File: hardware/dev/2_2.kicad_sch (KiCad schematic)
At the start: 10 parts, among them U4 KH-TYPE-C-16P, U6 CH572D, U8 HX_JN1_27-2X5P_ZZ_H4_9, X2 XTM20032000DT00351001

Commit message: add developemnt board and fix issue related to dual i2c access
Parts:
- added D3: USBLC6-2P6, usb_sp:SOT-666-6_L1.6-W1.2-P0.50-LS1.6-BL, symbol usb_sp:USBLC6-2P6_C2827693
- added U22, U33: HX_PH254-01-04-Z-L11_5_STRAIGHT_PIN_HEADER, usb_sp_dev:HDR-TH_4P-HX-PH254-01-04-Z-L11.5, symbol usb_sp_dev:HX_PH254-01-04-Z-L11_5_STRAIGHT_PIN_HEADER
- added U24, U25: RH-5015, usb_sp_dev:SMD_RH-5015, symbol usb_sp_dev:RH-5015
- added U27: DMG2305UX-7, usb_sp_dev:SOT-23-3_L2.9-W1.3-P1.90-LS2.4-BR, symbol usb_sp_dev:DMG2305UX-7
- P2: renamed from U8; value HX_JN1_27-2X5P_ZZ_H4_9 -> HDR-IDC-2_54-2X5P; footprint usb_sp_fp:CONN-TH_10P-P1.27_HX-JN1.27-2X5P-ZZ-H4.9 -> usb_sp:IDC-TH_10P-P2.54_C5665; symbol usb_sp:HX_JN1_27-2X5P_ZZ_H4_9 -> usb_sp:HDR-IDC-2_54-2X5P; LCSC C42372547 -> C5665
- U20: renamed from BOOT_1; value ~ -> TC-6601-5_0-260-8_3; footprint usb_sp_fp:SW-SMD_L3.9-W3.0-P4.45 -> usb_sp_dev:SW-SMD_4P-L6.0-W6.0-P4.50-LS8.2; symbol usb_sp:TS-1088-AR02016 -> usb_sp_dev:TC-6601-5_0-260-8_3; LCSC C720477 -> C7528752
- U21: renamed from U6; footprint usb_sp_fp:QFN-20_L3.0-W3.0-P0.40-TL-EP1.7 -> usb_sp:QFN-20_L3.0-W3.0-P0.40-TL-EP1.7
- U23: renamed from U4; footprint usb_sp_fp:USB-C-SMD_KH-TYPE-C-16P -> usb_sp:USB-C-SMD_KH-TYPE-C-16P
- X2: footprint usb_sp_fp:CRYSTAL-SMD_4P-L2.0-W1.6-BL -> usb_sp:CRYSTAL-SMD_4P-L2.0-W1.6-BL
- renumbered C14 to C13, C12 to C14, R1 to R10, R2 to R11, R3 to R12
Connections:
- net BOOT_0: now also D3.4 (I/O2), U33.2; no longer U23.A6 (DP1), U23.B6 (DP2)
- net GND: now also D3.2 (GND), U27.1 (G), U33.1
- net RST_CH572: now also U33.4
- net SPI_CLK: now also U22.3
- net SPI_CS: now also U22.4
- net SPI_MISO: now also U22.2
- net SPI_MOSI: now also U22.1
- net SWDIO: now also D3.6 (I/O1), U33.3; no longer U23.A7 (DN1), U23.B7 (DN2)
- net VBUS: now also D3.5 (VBUS), U27.2 (S); no longer U23.A4 (VBUS), U23.A9 (VBUS), U23.B4 (VBUS), U23.B9 (VBUS)
- net XI: now also U24.1
- net XO: now also U25.1
- net at U20.2: no longer R10.1
- new net: R10.1, U20.3
- new net D+: D3.3 (I/O2), U23.A6 (DP1), U23.B6 (DP2)
- new net D-: D3.1 (I/O1), U23.A7 (DN1), U23.B7 (DN2)
- new net USB_2_VBUS: U23.A4 (VBUS), U23.A9 (VBUS), U23.B4 (VBUS), U23.B9 (VBUS), U27.3 (D)
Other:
- moved on the sheet: R11, R12

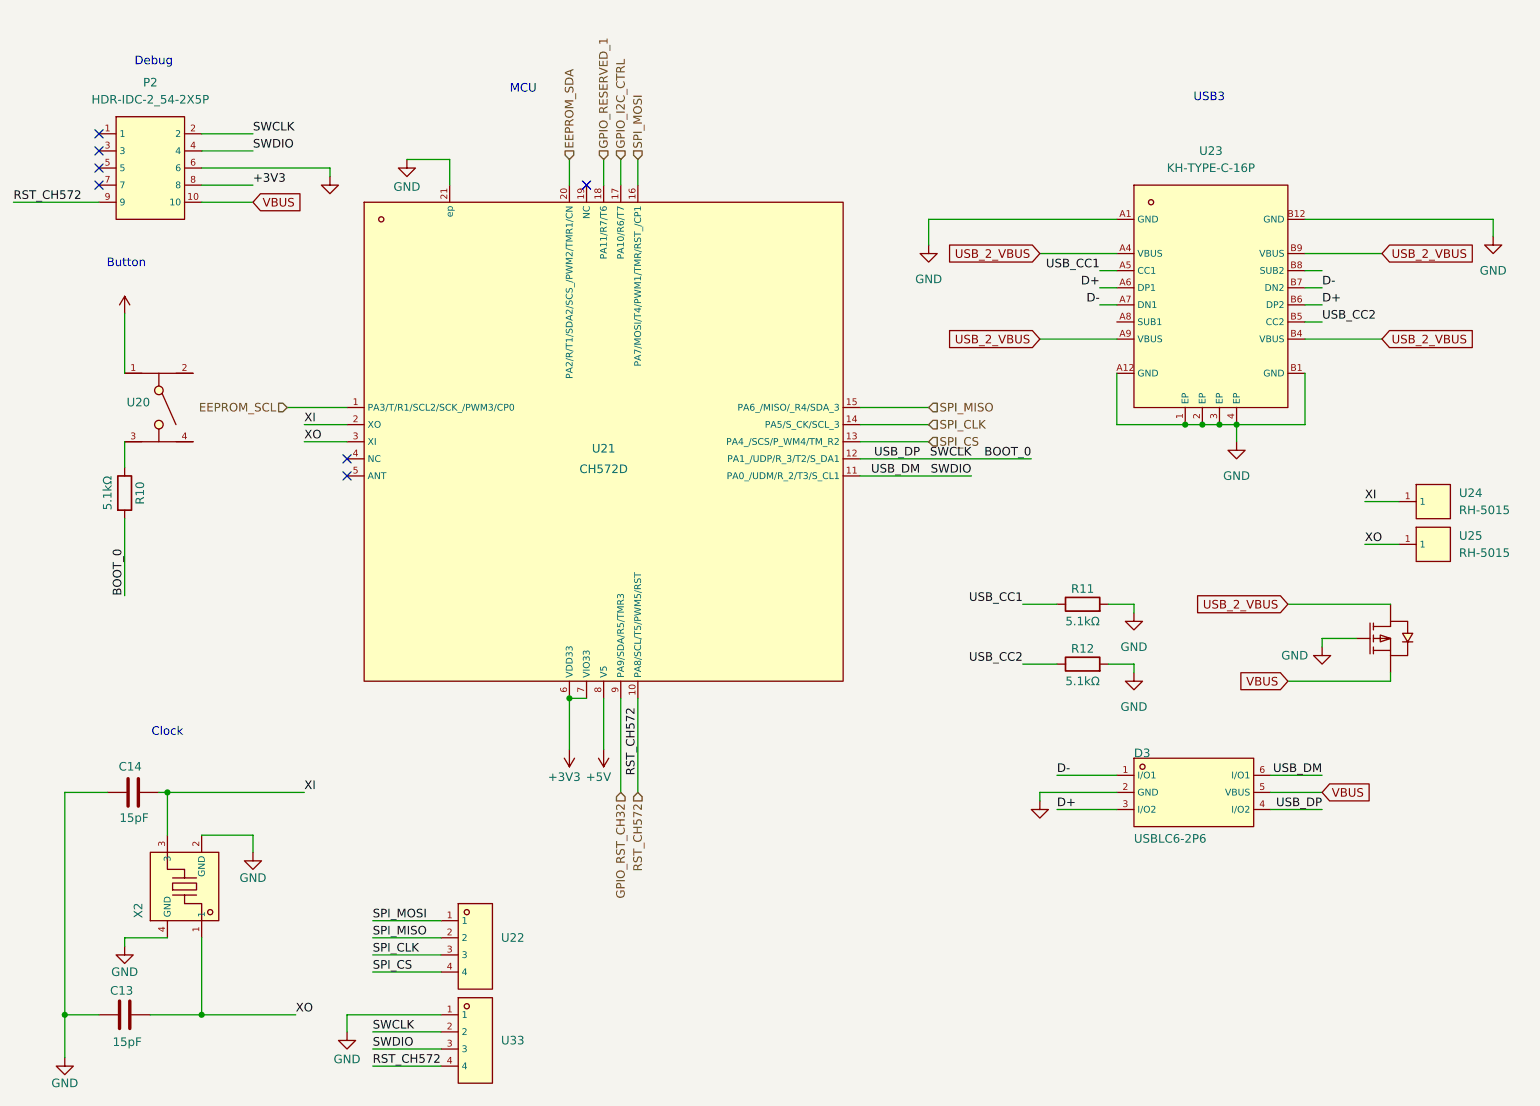
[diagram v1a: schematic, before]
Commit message: feat(hardware-dev): replace mode transistors with TPS2121 power mux
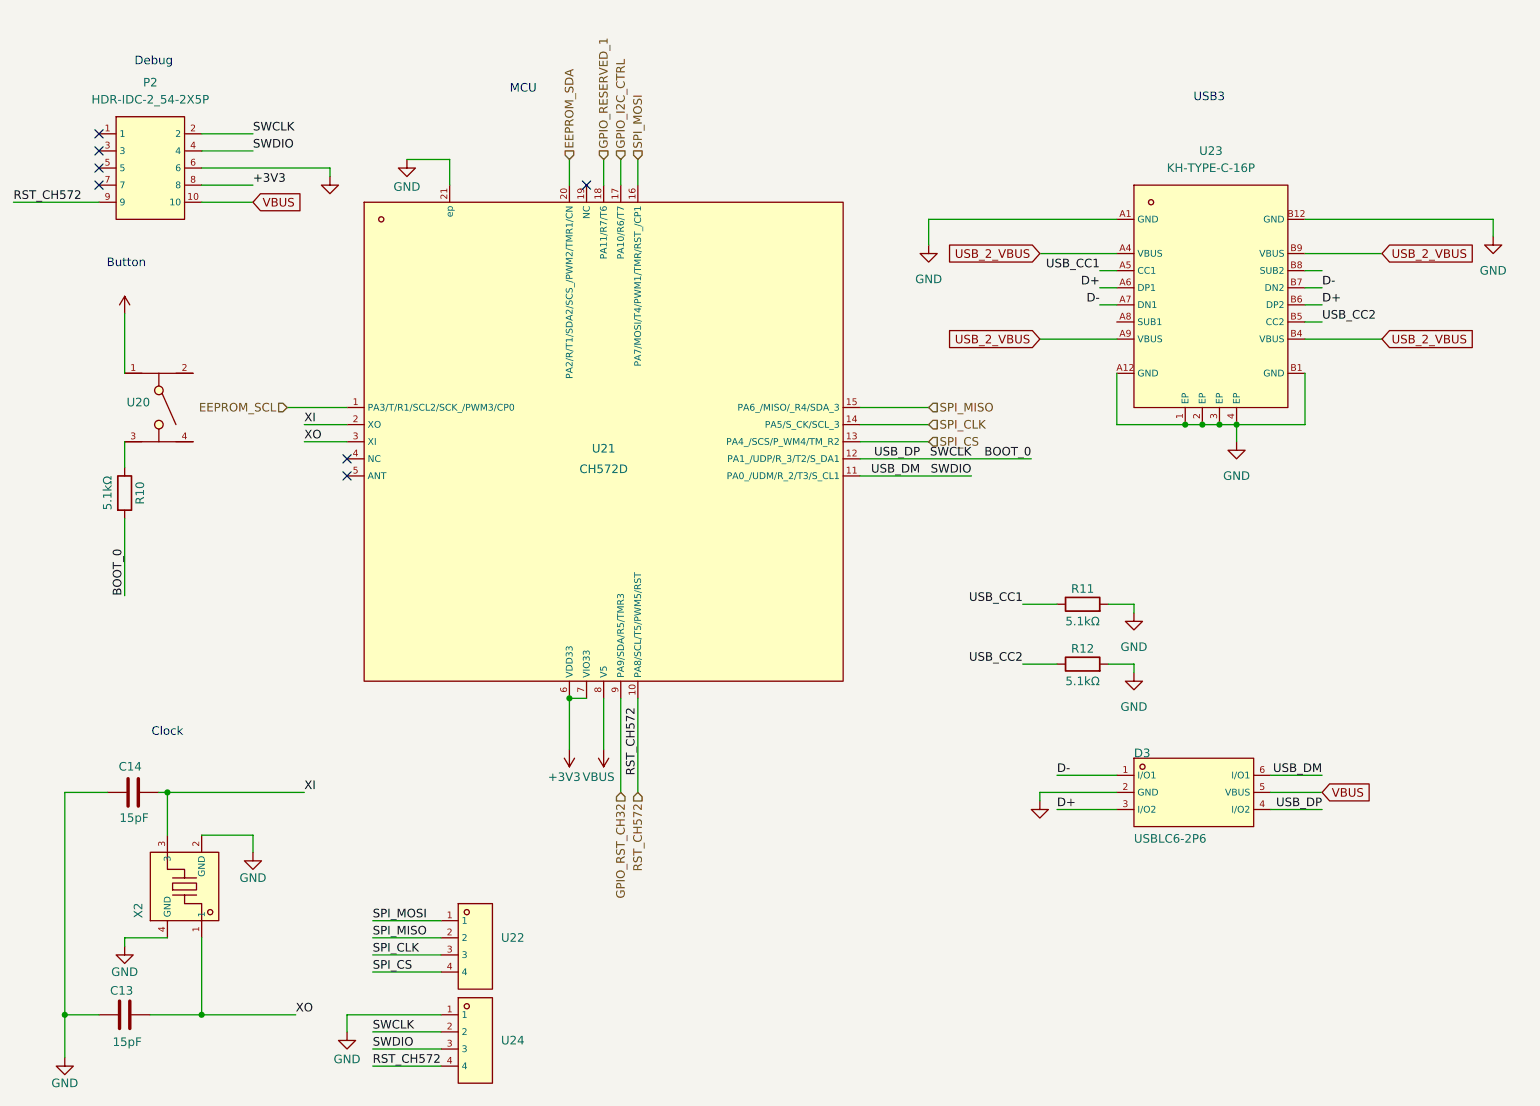
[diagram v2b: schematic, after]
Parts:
- removed U24, U25: RH-5015, usb_sp_dev:SMD_RH-5015, symbol usb_sp_dev:RH-5015
- removed U27: DMG2305UX-7, usb_sp_dev:SOT-23-3_L2.9-W1.3-P1.90-LS2.4-BR, symbol usb_sp_dev:DMG2305UX-7
- renumbered U33 to U24
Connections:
- net +5V is gone; now on net VBUS: U21.8 (V5)
